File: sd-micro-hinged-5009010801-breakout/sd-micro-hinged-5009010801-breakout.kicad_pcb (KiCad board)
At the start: 2 copper layers, 0 parts

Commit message: Release v1.0 Hinged Micro SD Breakout
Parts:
- added C1: 1uF, Wickerlib:RLC-0603-SMD, F.Cu at (117.1, 106.0)
- added C2: 0.1uF, Wickerlib:RLC-0603-SMD, F.Cu at (117.8, 103.3)
- added C3: 0.1uF, Wickerlib:RLC-0603-SMD, F.Cu at (122.4, 103.3)
- added C4: 1uF, Wickerlib:RLC-0603-SMD, F.Cu at (122.1, 106.1)
- added J1: BREAKOUT, Wickerlib:CONN-HEADER-STRAIGHT-P2.54MM-1x06, F.Cu at (109.5, 106.7)
- added J2: CONN-MICRO-SD-CARD-HINGED-TYPE, Wickerlib:CONN-SD-MICRO-MOLEX-5009010801, F.Cu at (134.6, 99.3)
- added U1: MIC5365 150mA, Wickerlib:SOT-353, F.Cu at (119.6, 106.1)
- added U2: TXB0104, Wickerlib:SOIC-14-3.9x8.7MM-P1.27MM, F.Cu at (119.5, 96.9)
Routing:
- net GND: track 0.00 -> 73.6 mm, vias 0 -> 1
- net +3V3: track 0.00 -> 33.9 mm, vias 0 -> 2
- net VIN: track 0.00 -> 17.3 mm
- net /MISO: track 0.00 -> 9.34 mm
- net /CLK: track 0.00 -> 8.81 mm
- net /SD_MISO: track 0.00 -> 8.57 mm
- net /MOSI: track 0.00 -> 8.20 mm
- net /SD_CLK: track 0.00 -> 8.18 mm
- net /SD_CS: track 0.00 -> 7.87 mm
- net /SD_MOSI: track 0.00 -> 7.80 mm
- net /CS: track 0.00 -> 7.67 mm
- added copper zone on B.Cu, net GND
- added copper zone on F.Cu, net GND
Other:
- board outline added: 31.8 x 17.8 mm
- rule pad_to_mask_clearance: 0.0762 -> 0.0508
- rule trace_clearance: 0.1524 -> 0.254
- board text added: "CS"
- board text added: "GND"
- board text added: "Hinged Micro SD Card Breakout"
- board text added: "MISO"
- board text added: "MOSI"
- board text added: "SCK"
- board text added: "SD Connector: Molex P/N 5009010801 VIN can be 5V or 3.3V wickerbox.net"
- board text added: "VIN"

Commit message: Release v1.0 MicroSD Push-Pull Breakout
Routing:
- net GND: track 73.6 -> 75.5 mm, vias 1 -> 2
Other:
- board text added: "1/3/16"
- board text added: "Hinged Micro SD Card Breakout v1.0"
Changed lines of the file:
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@@
     (area 104.572999 74.854999 178.510001 123.265001)
     (thickness 1.6)
-    (drawings 34)
-    (tracks 90)
+    (drawings 44)
+    (tracks 93)
     (zones 0)
     (modules 8)
@@
   )
   (setup
-    (last_trace_width 0.508)
+    (last_trace_width 0.254)
     (user_trace_width 0.1524)
     (user_trace_width 0.254)
@@
     (add_net VIN)
   )
+  (module Wickerlib:CONN-SD-MICRO-MOLEX-5009010801 (layer F.Cu)
+    (at 134.567 99.3405 90)
+    (fp_text reference J2 (at -0.545 -2.1695 180) (layer F.Fab)
+      (effects (font (size 1.016 1.016) (thickness 0.2032)))
+    )
+    (fp_text value CONN-MICRO-SD-CARD-HINGED-TYPE (at 0.3 -11.1 90) (layer F.Fab) hide
+      (effects (font (size 1.016 1.016) (thickness 0.1524)))
+    )
+    (fp_line (start 7.25 3.75) (end 7.25 -10.25) (layer F.Fab) (width 0.04064))
+    (fp_line (start -8.5 3.75) (end 7.25 3.75) (layer F.Fab) (width 0.04064))
+    (fp_line (start -8.5 -10.25) (end -8.5 3.75) (layer F.Fab) (width 0.04064))
+    (fp_line (start -6 -10.25) (end -8.5 -10.25) (layer F.Fab) (width 0.04064))
+    (fp_line (start -6 -9) (end -6 -10.25) (layer F.Fab) (width 0.04064))
+    (fp_line (start 3.5 -9) (end -6 -9) (layer F.Fab) (width 0.04064))
+    (fp_line (start 3.5 -10.25) (end 3.5 -9) (layer F.Fab) (width 0.04064))
+    (fp_line (start 7.25 -10.25) (end 3.5 -10.25) (layer F.Fab) (width 0.04064))
+    (fp_line (start 7.25 3.75) (end 7.25 -10) (layer F.CrtYd) (width 0.04064))
+    (fp_line (start -8.5 3.75) (end 7.25 3.75) (layer F.CrtYd) (width 0.04064))
+    (fp_line (start -8.5 -10.25) (end -8.5 3.75) (layer F.CrtYd) (width 0.04064))
+    (fp_line (start 7.25 -10.25) (end -8.5 -10.25) (layer F.CrtYd) (width 0.04064))
+    (fp_line (start 7.25 -10) (end 7.25 -10.25) (layer F.CrtYd) (width 0.04064))
+    (fp_text user %R (at -8.3555 2.212 180) (layer F.SilkS)
+      (effects (font (size 1 1) (thickness 0.15)))
+    )
+    (fp_text user 1 (at 4 -6.9 90) (layer F.SilkS)
+      (effects (font (size 1 1) (thickness 0.15)))
+    )
+    (fp_line (start -7.5 3.6) (end 6 3.6) (layer F.SilkS) (width 0.1016))
+    (fp_line (start 6 -10) (end 6 -9.7) (layer F.SilkS) (width 0.1016))
+    (fp_line (start 3.7 -10) (end 6 -10) (layer F.SilkS) (width 0.1016))
+    (fp_line (start 3.7 -8.9) (end 3.7 -10) (layer F.SilkS) (width 0.1016))
+    (fp_line (start -6 -8.9) (end 3.7 -8.9) (layer F.SilkS) (width 0.1016))
+    (fp_line (start -6 -10) (end -6 -8.9) (layer F.SilkS) (width 0.1016))
+    (fp_line (start -7.5 -10) (end -6 -10) (layer F.SilkS) (width 0.1016))
+    (fp_line (start -7.5 -9.7) (end -7.5 -10) (layer F.SilkS) (width 0.1016))
+    (fp_line (start -7.5 3.6) (end -7.5 -9.7) (layer F.SilkS) (width 0.1016))
+    (fp_line (start 6 3.6) (end 6 -9.7) (layer F.SilkS) (width 0.1016))
+    (pad 6 smd rect (at 6.1 0 90) (size 1.45 2) (layers F.Cu F.Paste F.Mask)
+      (net 2 GND))
+    (pad 6 smd rect (at -7.5 0 90) (size 1.45 2) (layers F.Cu F.Paste F.Mask)
+      (net 2 GND))
+    (pad 6 smd rect (at 6.1 -8.3 90) (size 1.45 2) (layers F.Cu F.Paste F.Mask)
+      (net 2 GND))
+    (pad 6 smd rect (at -7.5 -8.3 90) (size 1.45 2) (layers F.Cu F.Paste F.Mask)
+      (net 2 GND))
+    (pad 7 smd rect (at -2.7 -4.9 90) (size 0.7 1.6) (layers F.Cu F.Paste F.Mask)
+      (net 8 /SD_MISO))
+    (pad 8 smd rect (at -3.8 -4.9 90) (size 0.7 1.6) (layers F.Cu F.Paste F.Mask))
+    (pad 6 smd rect (at -1.6 -4.9 90) (size 0.7 1.6) (layers F.Cu F.Paste F.Mask)
+      (net 2 GND))
+    (pad 5 smd rect (at -0.5 -4.9 90) (size 0.7 1.6) (layers F.Cu F.Paste F.Mask)
+      (net 9 /SD_CLK))
+    (pad 4 smd rect (at 0.6 -4.9 90) (size 0.7 1.6) (layers F.Cu F.Paste F.Mask)
+      (net 3 +3V3))
+    (pad 1 smd rect (at 3.9 -4.9 90) (size 0.7 1.6) (layers F.Cu F.Paste F.Mask))
+    (pad 2 smd rect (at 2.8 -4.9 90) (size 0.7 1.6) (layers F.Cu F.Paste F.Mask)
+      (net 10 /SD_CS))
+    (pad 3 smd rect (at 1.7 -4.9 90) (size 0.7 1.6) (layers F.Cu F.Paste F.Mask)
+      (net 11 /SD_MOSI))
+  )
   (module Wickerlib:RLC-0603-SMD (layer F.Cu)
     (at 117.094 106.045 270)
@@
     (pad 6 thru_hole oval (at 0 12.7 180) (size 2.032 1.7272) (drill 1.016) (layers *.Cu *.Mask F.SilkS)
       (net 2 GND))
-  )
-  (module Wickerlib:CONN-SD-MICRO-MOLEX-5009010801 (layer F.Cu)
-    (at 134.567 99.3405 90)
-    (fp_text reference J2 (at -0.545 -2.1695 180) (layer F.Fab)
-      (effects (font (size 1.016 1.016) (thickness 0.2032)))
-    )
-    (fp_text value CONN-MICRO-SD-CARD-HINGED-TYPE (at 0.3 -11.1 90) (layer F.Fab) hide
-      (effects (font (size 1.016 1.016) (thickness 0.1524)))
-    )
-    (fp_line (start 7.25 3.75) (end 7.25 -10.25) (layer F.Fab) (width 0.04064))
-    (fp_line (start -8.5 3.75) (end 7.25 3.75) (layer F.Fab) (width 0.04064))
-    (fp_line (start -8.5 -10.25) (end -8.5 3.75) (layer F.Fab) (width 0.04064))
-    (fp_line (start -6 -10.25) (end -8.5 -10.25) (layer F.Fab) (width 0.04064))
-    (fp_line (start -6 -9) (end -6 -10.25) (layer F.Fab) (width 0.04064))
-    (fp_line (start 3.5 -9) (end -6 -9) (layer F.Fab) (width 0.04064))
-    (fp_line (start 3.5 -10.25) (end 3.5 -9) (layer F.Fab) (width 0.04064))
-    (fp_line (start 7.25 -10.25) (end 3.5 -10.25) (layer F.Fab) (width 0.04064))
-    (fp_line (start 7.25 3.75) (end 7.25 -10) (layer F.CrtYd) (width 0.04064))
-    (fp_line (start -8.5 3.75) (end 7.25 3.75) (layer F.CrtYd) (width 0.04064))
-    (fp_line (start -8.5 -10.25) (end -8.5 3.75) (layer F.CrtYd) (width 0.04064))
-    (fp_line (start 7.25 -10.25) (end -8.5 -10.25) (layer F.CrtYd) (width 0.04064))
-    (fp_line (start 7.25 -10) (end 7.25 -10.25) (layer F.CrtYd) (width 0.04064))
-    (fp_text user %R (at -8.3555 2.212 180) (layer F.SilkS)
-      (effects (font (size 1 1) (thickness 0.15)))
-    )
-    (fp_text user 1 (at 4 -6.9 90) (layer F.SilkS)
-      (effects (font (size 1 1) (thickness 0.15)))
-    )
-    (fp_line (start -7.5 3.6) (end 6 3.6) (layer F.SilkS) (width 0.1016))
-    (fp_line (start 6 -10) (end 6 -9.7) (layer F.SilkS) (width 0.1016))
-    (fp_line (start 3.7 -10) (end 6 -10) (layer F.SilkS) (width 0.1016))
-    (fp_line (start 3.7 -8.9) (end 3.7 -10) (layer F.SilkS) (width 0.1016))
-    (fp_line (start -6 -8.9) (end 3.7 -8.9) (layer F.SilkS) (width 0.1016))
-    (fp_line (start -6 -10) (end -6 -8.9) (layer F.SilkS) (width 0.1016))
-    (fp_line (start -7.5 -10) (end -6 -10) (layer F.SilkS) (width 0.1016))
-    (fp_line (start -7.5 -9.7) (end -7.5 -10) (layer F.SilkS) (width 0.1016))
-    (fp_line (start -7.5 3.6) (end -7.5 -9.7) (layer F.SilkS) (width 0.1016))
-    (fp_line (start 6 3.6) (end 6 -9.7) (layer F.SilkS) (width 0.1016))
-    (pad 6 smd rect (at 6.1 0 90) (size 1.45 2) (layers F.Cu F.Paste F.Mask)
-      (net 2 GND))
-    (pad 6 smd rect (at -7.5 0 90) (size 1.45 2) (layers F.Cu F.Paste F.Mask)
-      (net 2 GND))
-    (pad 6 smd rect (at 6.1 -8.3 90) (size 1.45 2) (layers F.Cu F.Paste F.Mask)
-      (net 2 GND))
-    (pad 6 smd rect (at -7.5 -8.3 90) (size 1.45 2) (layers F.Cu F.Paste F.Mask)
-      (net 2 GND))
-    (pad 7 smd rect (at -2.7 -4.9 90) (size 0.7 1.6) (layers F.Cu F.Paste F.Mask)
-      (net 8 /SD_MISO))
-    (pad 8 smd rect (at -3.8 -4.9 90) (size 0.7 1.6) (layers F.Cu F.Paste F.Mask))
-    (pad 6 smd rect (at -1.6 -4.9 90) (size 0.7 1.6) (layers F.Cu F.Paste F.Mask)
-      (net 2 GND))
-    (pad 5 smd rect (at -0.5 -4.9 90) (size 0.7 1.6) (layers F.Cu F.Paste F.Mask)
-      (net 9 /SD_CLK))
-    (pad 4 smd rect (at 0.6 -4.9 90) (size 0.7 1.6) (layers F.Cu F.Paste F.Mask)
-      (net 3 +3V3))
-    (pad 1 smd rect (at 3.9 -4.9 90) (size 0.7 1.6) (layers F.Cu F.Paste F.Mask))
-    (pad 2 smd rect (at 2.8 -4.9 90) (size 0.7 1.6) (layers F.Cu F.Paste F.Mask)
-      (net 10 /SD_CS))
-    (pad 3 smd rect (at 1.7 -4.9 90) (size 0.7 1.6) (layers F.Cu F.Paste F.Mask)
-      (net 11 /SD_MOSI))
   )
   (module Wickerlib:SOIC-14-3.9x8.7MM-P1.27MM (layer F.Cu)
@@
     )
   )
-  (gr_circle (center 123.698 100.838) (end 123.952 100.838) (layer F.SilkS) (width 0.1524))
+  (gr_text 1/3/16 (at 134.112 110.998) (layer F.Fab)
+    (effects (font (size 1.016 1.016) (thickness 0.1524)))
+  )
+  (gr_text "Hinged Micro SD Card Breakout v1.0" (at 122.936 89.662) (layer F.Fab)
+    (effects (font (size 1.016 1.016) (thickness 0.1524)))
+  )
   (gr_text "Hinged Micro SD Card Breakout" (at 124.714 94.234) (layer B.SilkS)
     (effects (font (size 1.016 1.016) (thickness 0.1524)) (justify mirror))
   )
+  (gr_circle (center 123.698 100.838) (end 123.952 100.838) (layer F.SilkS) (width 0.1524))
   (gr_text "SD Connector:\nMolex P/N 5009010801\n\nVIN can be 5V or 3.3V\n\nwickerbox.net" (at 125.222 102.108) (layer B.SilkS)
     (effects (font (size 1.016 1.016) (thickness 0.1524)) (justify mirror))
@@
   (segment (start 115.3802 105.295) (end 117.094 105.295) (width 0.508) (layer F.Cu) (net 1))
   (segment (start 109.474 106.68) (end 113.9952 106.68) (width 0.508) (layer F.Cu) (net 1))
+  (segment (start 129.667 100.9405) (end 127.8645 100.9405) (width 0.254) (layer F.Cu) (net 2))
+  (segment (start 127.8645 100.9405) (end 127.762 100.838) (width 0.254) (layer F.Cu) (net 2))
+  (via (at 127.762 100.838) (size 0.6858) (drill 0.3302) (layers F.Cu B.Cu) (net 2))
   (segment (start 120.142 103.3145) (end 118.594 103.3145) (width 0.508) (layer F.Cu) (net 2))
   (segment (start 121.6145 103.3145) (end 120.142 103.3145) (width 0.508) (layer F.Cu) (net 2))

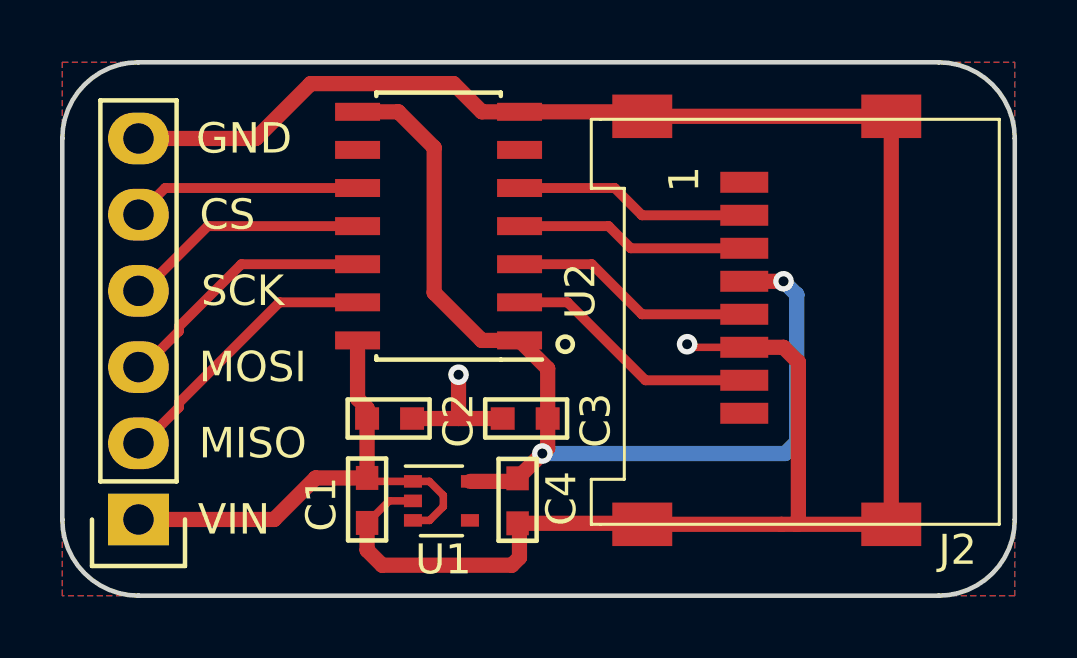
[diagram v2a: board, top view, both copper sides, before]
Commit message: Fix wiring. Add assy diagram. v1.1 release.
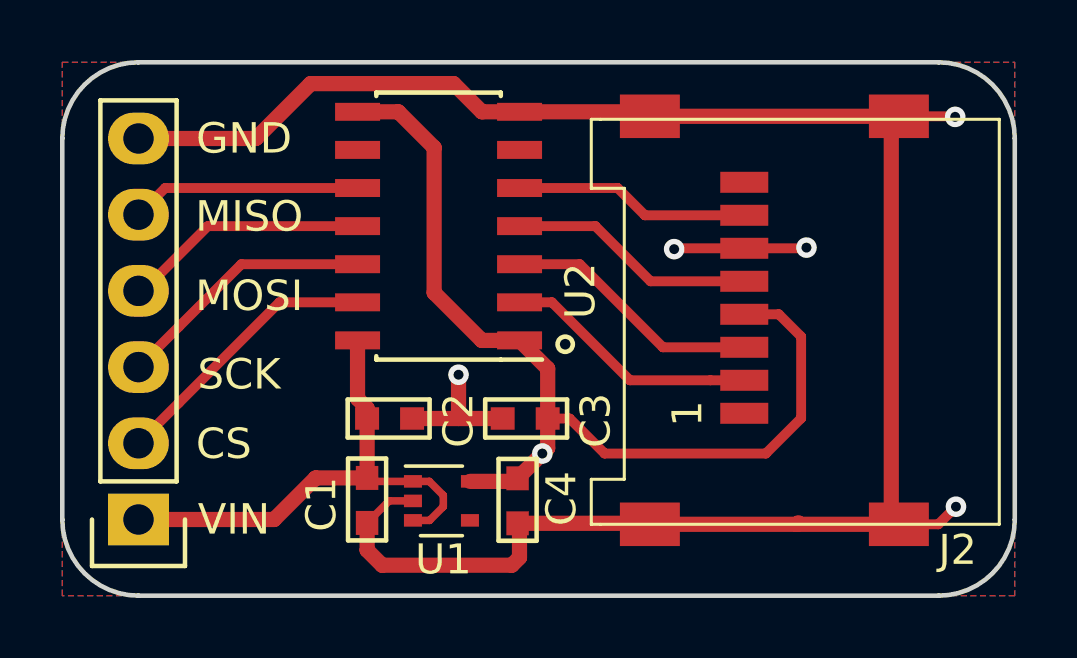
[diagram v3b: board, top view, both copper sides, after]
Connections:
- J1 pad 2: /MISO -> /CS
- J1 pad 3: /CLK -> /MOSI
- J1 pad 4: /MOSI -> /CLK
- J1 pad 5: /CS -> /MISO
- U2 pad 10: /CS -> /MISO
- U2 pad 11: /MOSI -> /CLK
- U2 pad 12: /CLK -> /MOSI
- U2 pad 13: /MISO -> /CS
- U2 pad 2: /SD_MISO -> /SD_CS
- U2 pad 3: /SD_CLK -> /SD_MOSI
- U2 pad 4: /SD_MOSI -> /SD_CLK
- U2 pad 5: /SD_CS -> /SD_MISO
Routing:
- net /CS: track 7.67 -> 9.40 mm
- net /MISO: track 9.34 -> 7.67 mm
- net +3V3: track 33.9 -> 32.8 mm, vias 2 -> 1
- net /SD_MOSI: track 7.80 -> 8.64 mm
- net /SD_MISO: track 8.57 -> 7.87 mm
- net /SD_CS: track 7.87 -> 8.57 mm
- net /MOSI: track 8.20 -> 8.88 mm
- net /CLK: track 8.81 -> 8.20 mm
- net GND: track 75.5 -> 75.2 mm, vias 2 -> 5
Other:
- board text added: "Hinged Micro SD Card Breakout v1.1"
- board text removed: "1/3/16"
- board text removed: "Hinged Micro SD Card Breakout"
- board text removed: "Hinged Micro SD Card Breakout v1.0"
